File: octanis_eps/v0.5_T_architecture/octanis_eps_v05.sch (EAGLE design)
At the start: 141 parts, among them IC1 OPA2333DGK, Q1 32.768kHz, Q100 BSS123, U1 CSD16327Q3_DQG_8, U10 CSD16327Q3_DQG_8, U100 Value, U11 CSD16327Q3_DQG_8, U2 CSD16327Q3_DQG_8, U3 CSD16327Q3_DQG_8, U4 MSP430G2544, U5 TPS2022D, U6 Value, U7 Value, U8 TPS61232, U9 BQ24650_RVA_16

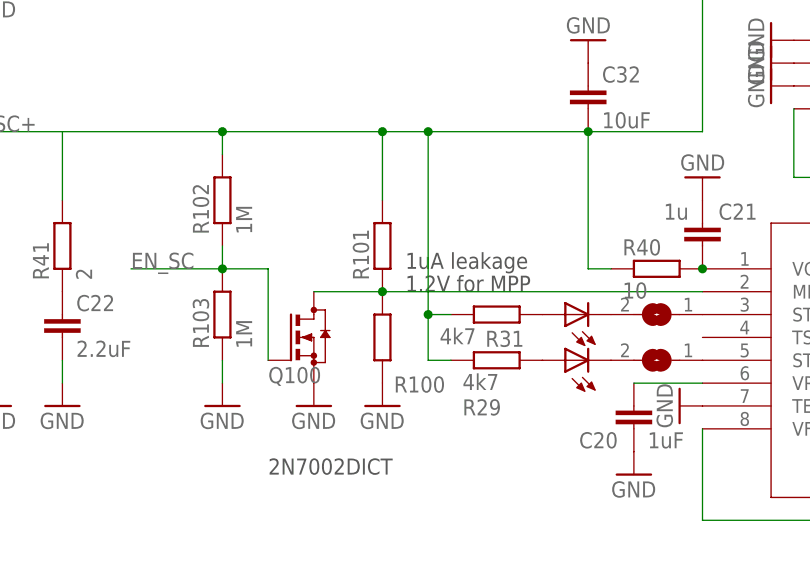
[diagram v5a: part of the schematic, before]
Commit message: adjusted final resistor values for eps v1.0
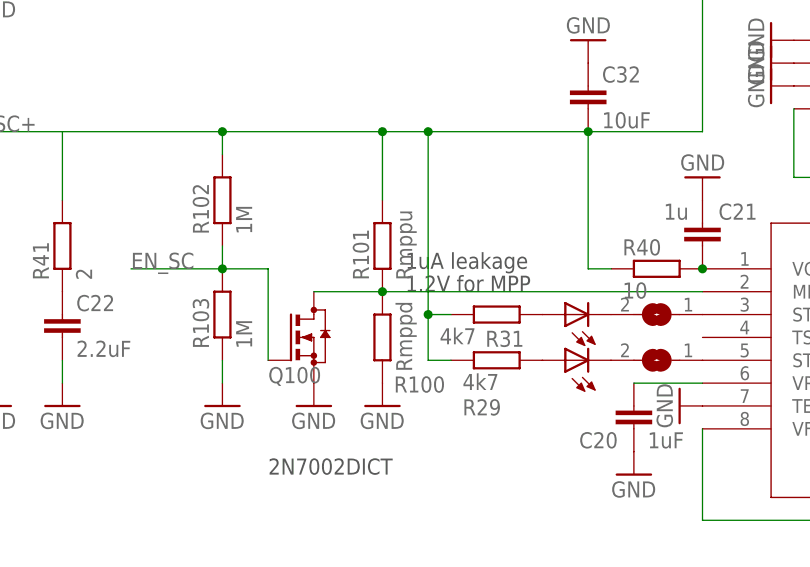
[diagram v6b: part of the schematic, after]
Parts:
- R100: value (none) -> Rmppd
- R101: value (none) -> Rmppu
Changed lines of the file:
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@@
 <part name="U10" library="texasinstruments" deviceset="CSD16327Q3_DQG_8" device=""/>
 <part name="U11" library="texasinstruments" deviceset="CSD16327Q3_DQG_8" device=""/>
-<part name="R101" library="rcl" deviceset="R-EU_" device="R0603"/>
-<part name="R100" library="rcl" deviceset="R-EU_" device="R0603"/>
+<part name="R101" library="rcl" deviceset="R-EU_" device="R0603" value="Rmppu"/>
+<part name="R100" library="rcl" deviceset="R-EU_" device="R0603" value="Rmppd"/>
 <part name="GND44" library="supply1" deviceset="GND" device=""/>
 <part name="R32" library="rcl" deviceset="R-EU_" device="R0603" value="100k"/>
